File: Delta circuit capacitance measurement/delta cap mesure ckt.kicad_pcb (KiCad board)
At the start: 2 copper layers, 81.8 x 64.5 mm, 10 parts, among them K4 CONN_3, P1 CONN_2, P2 CONN_4

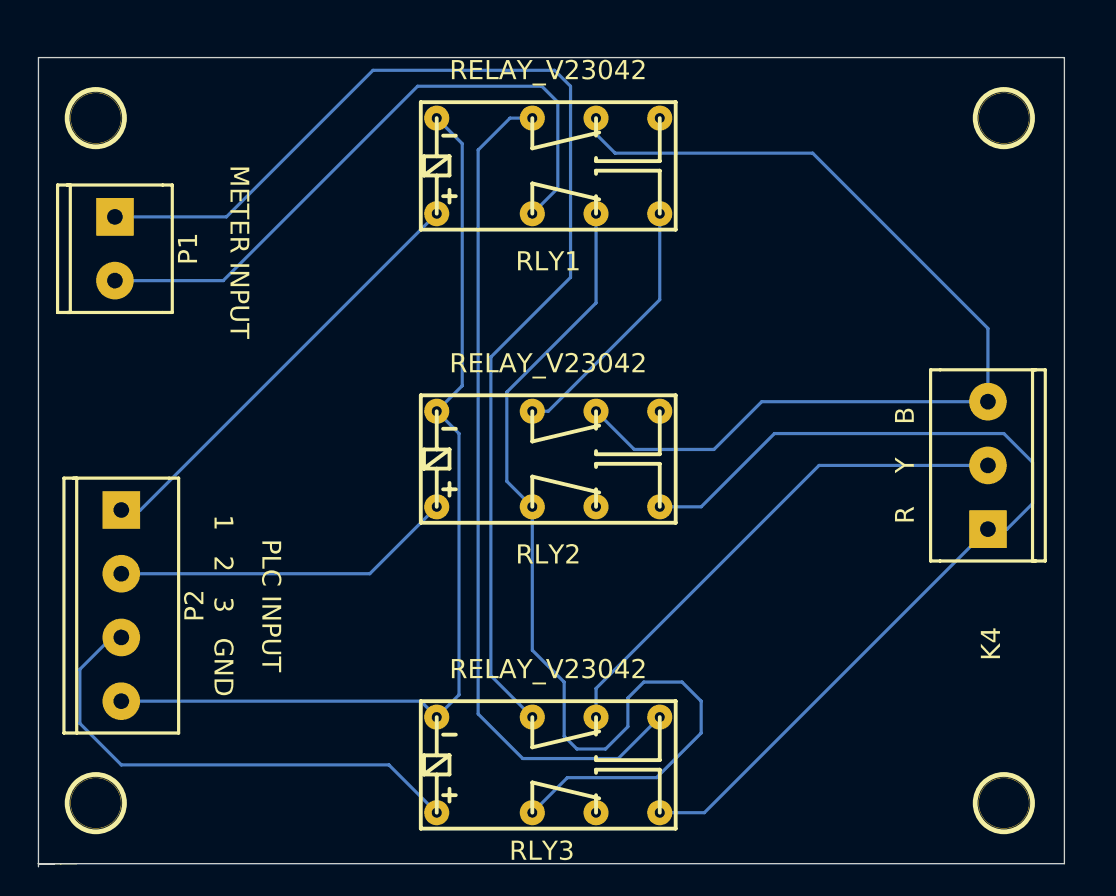
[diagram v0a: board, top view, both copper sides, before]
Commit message: Track width increased
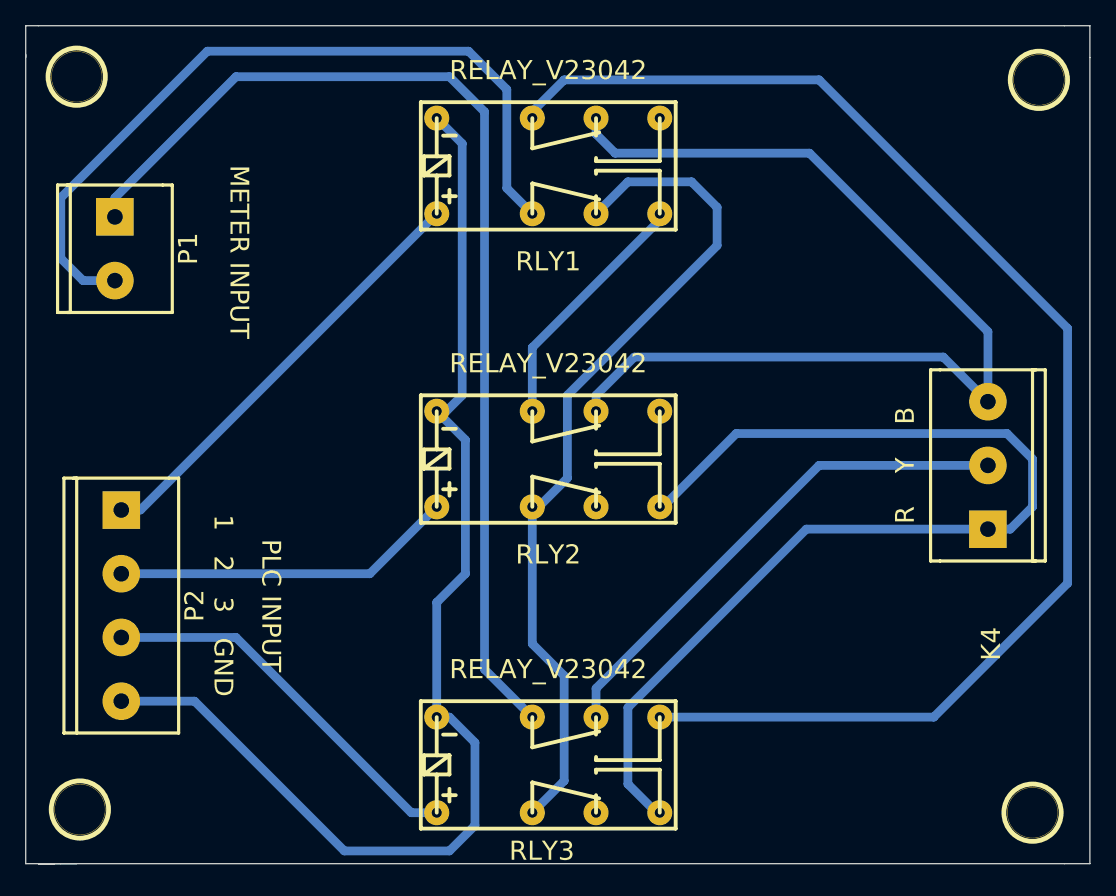
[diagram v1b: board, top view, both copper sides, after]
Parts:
- moved 1PIN 4.13 mm to (202.2, 102.4)
- moved 1PIN 3.64 mm to (125.5, 102.1)
- moved 1PIN 2.41 mm to (201.7, 160.8)
- moved 1PIN 1.37 mm to (125.7, 160.5)
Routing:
- net /R3_NO: track 67.6 -> 109.7 mm
- net /GND: track 76.6 -> 96.2 mm
- net /R1_NC: track 80.7 -> 68.3 mm
- net /M1: track 52.0 -> 62.3 mm
- net /M2: track 96.0 -> 86.0 mm
- net /K3: track 40.1 -> 30.9 mm
- net /B: track 76.3 -> 85.3 mm
- net /R: track 78.9 -> 79.9 mm
- net /R1_NC_R2_NC: track 20.7 -> 20.0 mm
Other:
- board size 81.8 x 64.5 mm -> 84.8 x 66.8 mm
- net class Default: trace_width 0.254 -> 0.7
